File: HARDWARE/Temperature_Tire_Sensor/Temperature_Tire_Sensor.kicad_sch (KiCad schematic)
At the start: 13 parts

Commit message: A completed schematic
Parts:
- added C?: 0.1uF, Capacitor_SMD:C_0603_1608Metric, symbol SB-Spoko-Bezpieczniki-rescue:C_Small-Device
- added D?: BLUE, symbol Device:D_Small
- added FB?: 60R@100MHz, symbol Device:FerriteBead_Small
- added J?: SWD_Conn_01x06, symbol Connector:Conn_01x06_Male
- added J?: CAN_Conn_01x02, symbol Connector_Generic:Conn_01x02
- added R?: 1k, symbol Device:R_Small_US
- added R?: 1k5, Resistor_SMD:R_0603_1608Metric, symbol SB-Spoko-Bezpieczniki-rescue:R_Small-Device
- added SW?: RESET, Button_Switch_THT:SW_PUSH_6mm, symbol SB-Spoko-Bezpieczniki-rescue:SW_Push-Switch
- C? (x2): value C_Small -> 8p
- R?: value R_Small_US -> 47
- Y?: value Crystal_GND24_Small -> 16MGHz
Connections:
- net +3V3: now also FB?.1, J?.1 (Pin_1); no longer C?.1, C?.1, C?.1, C?.1, C?.1, C?.1, C?.1
- net GND: now also C?.2, J?.3 (Pin_3), R?.2, SW?.1
- net LED: now reaches U?.26 (PB0)
- net LED: now also D?.2 (A)
- net CAN_RX: now reaches U?.44 (PA11)
- net CAN_TX: now reaches U?.45 (PA12)
- net SWDIO: now reaches U?.46 (PA13)
- net SWDIO: now also J?.4 (Pin_4)
- net SWCLK: now reaches U?.49 (PA14)
- net SWCLK: now also J?.2 (Pin_2)
- net SWO: now reaches U?.55 (PB3)
- net SWO: now also J?.6 (Pin_6)
- net NRST: now reaches U?.7 (NRST)
- net NRST: now also C?.1, J?.5 (Pin_5), R?.2
- net SCL: now reaches U?.8 (PC0)
- net SDA: now reaches U?.9 (PC1)
- new net: R?.1, SW?.2
- new net: C?.1, C?.1, C?.1, C?.1, C?.1, C?.1, C?.1, FB?.2
- new net: D?.1 (K), R?.1
- new net CAN_H: J?.1 (Pin_1)
- new net CAN_L: J?.2 (Pin_2)
- no-connect marks 0 -> 41
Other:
- sheet Power Supply 3V3 2V6 ports: added none; removed RO
- note added: "CAN"
- note added: "CRYSTAL"
- note added: "DIODE"
- note added: "POWER FILTRATION"
- note added: "POWER SUPPLY"
- note added: "RESET"
- note added: "STM32"
- note added: "SWD AND CAN CONNECTORS"
- note added: "TEMPERATURE SENSOR"
- moved on the sheet: C?, R?, U?, Y?

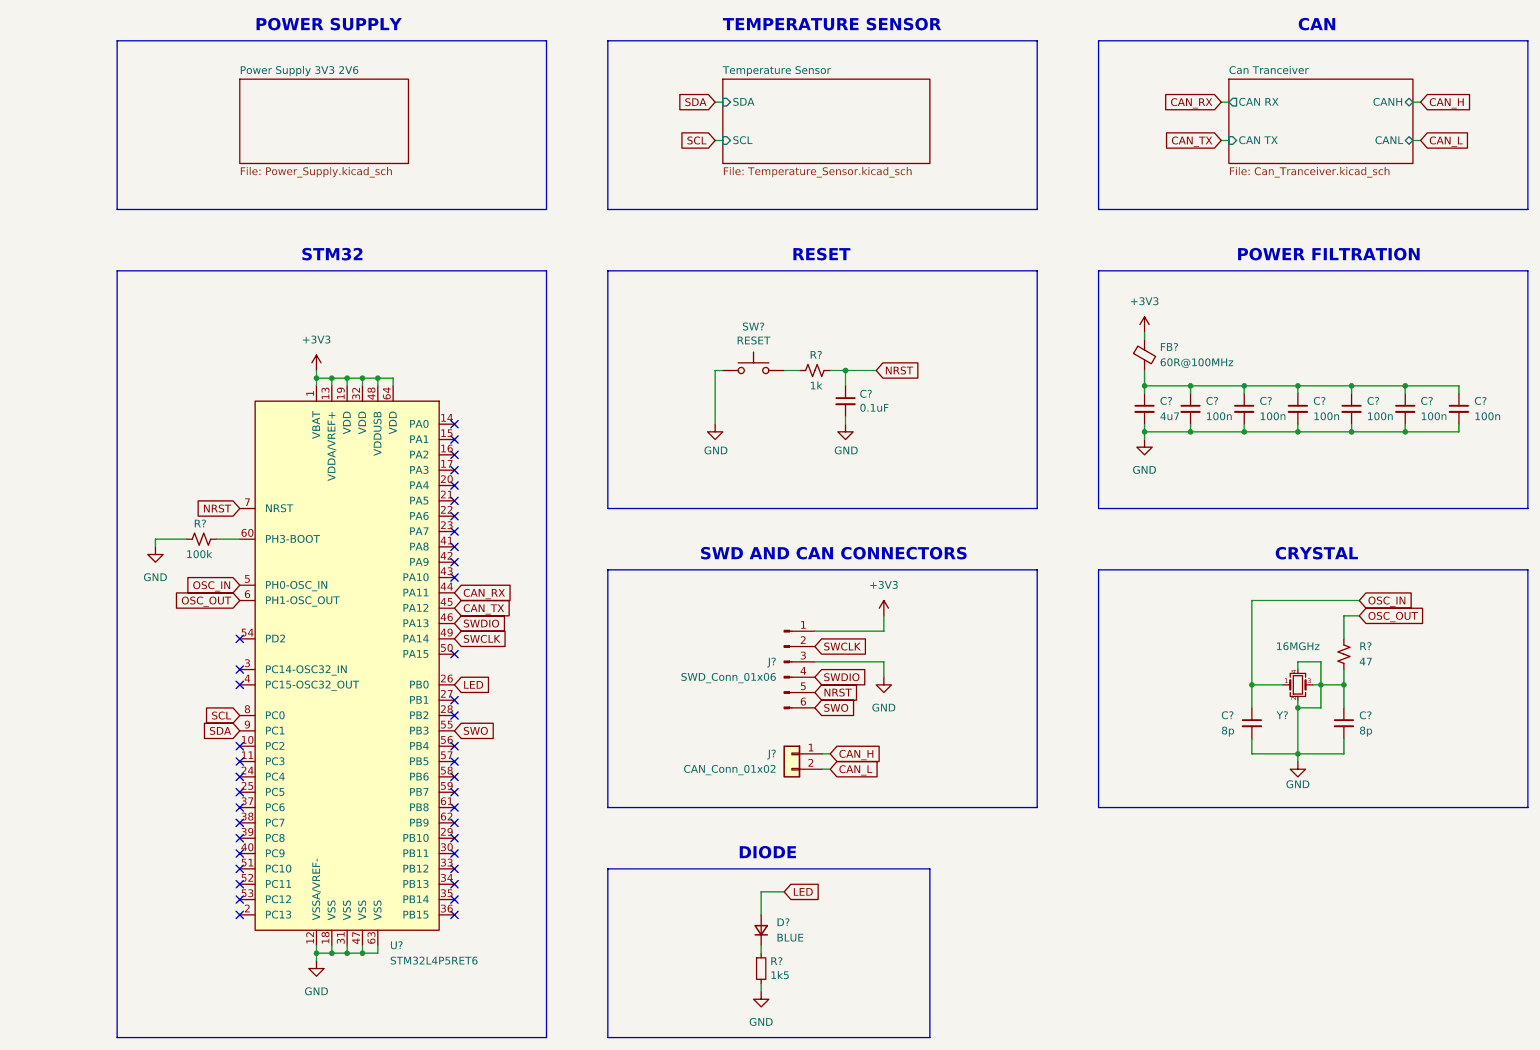
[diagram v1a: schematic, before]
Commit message: Changed the used type of labels and added power flags
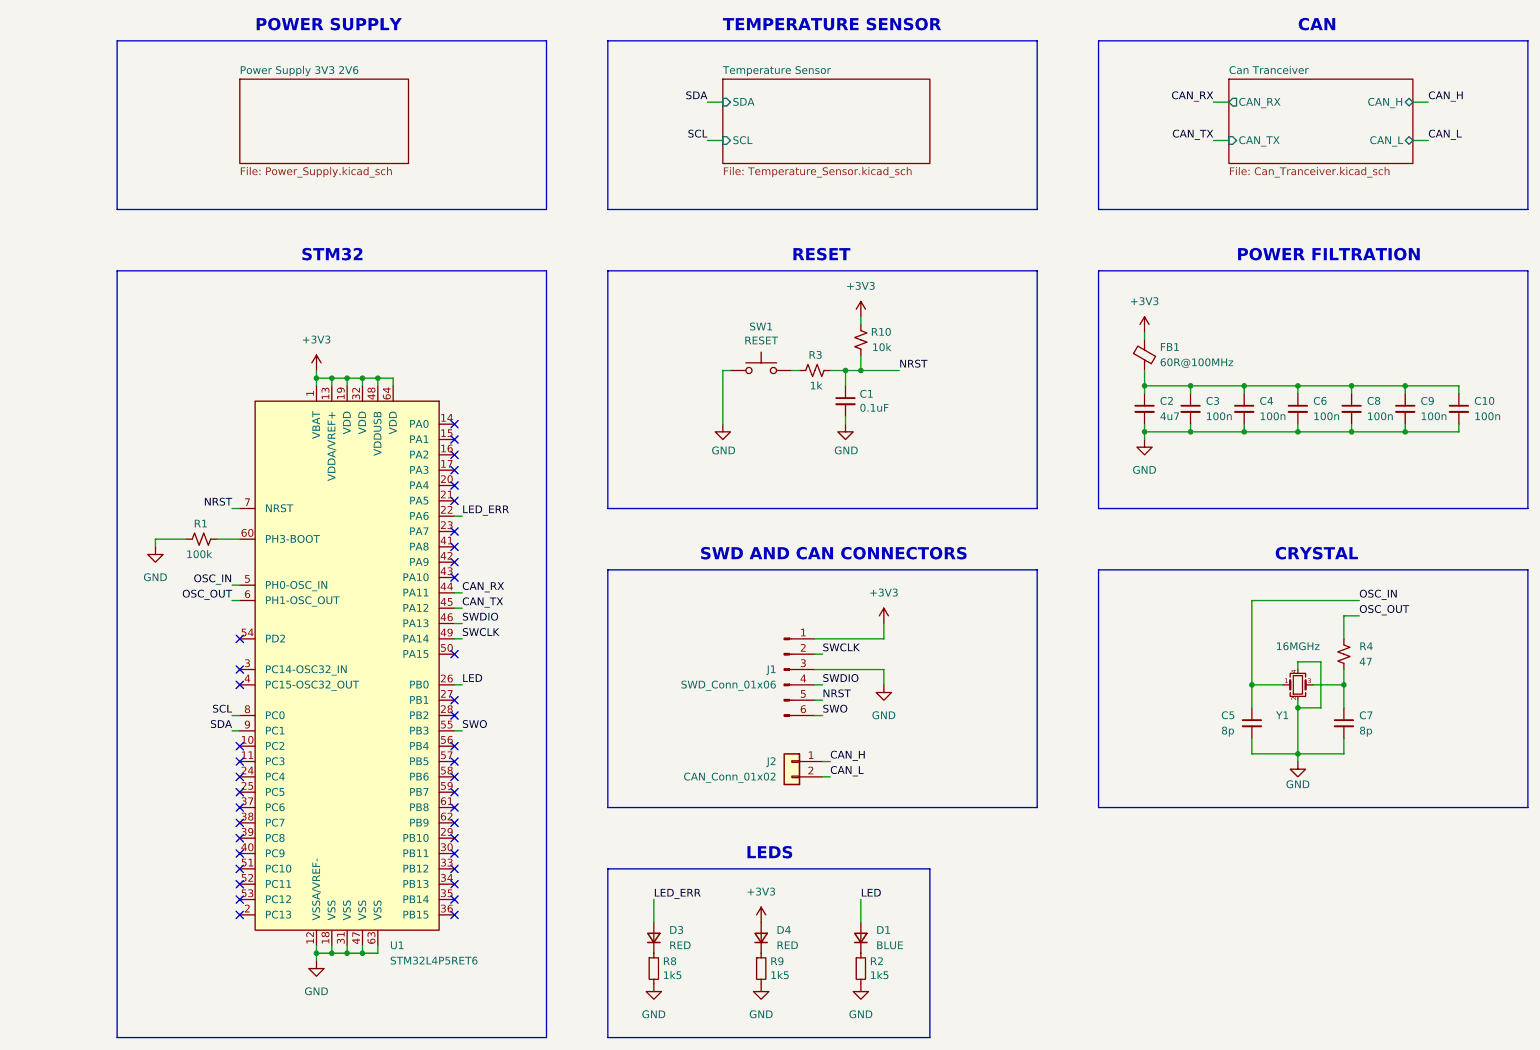
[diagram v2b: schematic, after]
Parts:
- added D3, D4: RED, symbol Device:D_Small
- added R10: 10k, symbol Device:R_Small_US
- added R8, R9: 1k5, Resistor_SMD:R_0603_1608Metric, symbol SB-Spoko-Bezpieczniki-rescue:R_Small-Device
- gave numbers to parts that had none: 21
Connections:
- net +3V3: now also D4.2 (A), R10.2
- net GND: now also R8.2, R9.2; no longer C7.1, R4.2, Y1.3
- net NRST: now also R10.1
- net LED_ERR: now reaches U1.22 (PA6)
- net LED_ERR: now also D3.2 (A)
- new net: C7.1, R4.2, Y1.3
- new net: D4.1 (K), R9.1
- new net: D3.1 (K), R8.1
- no-connect marks 41 -> 40
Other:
- sheet Can Tranceiver ports: added CAN_H, CAN_L, CAN_RX, CAN_TX; removed CAN RX, CAN TX, CANH, CANL
- note added: "LEDS"
- note removed: "DIODE"
- moved on the sheet: D1, J1, J2, R2, SW1

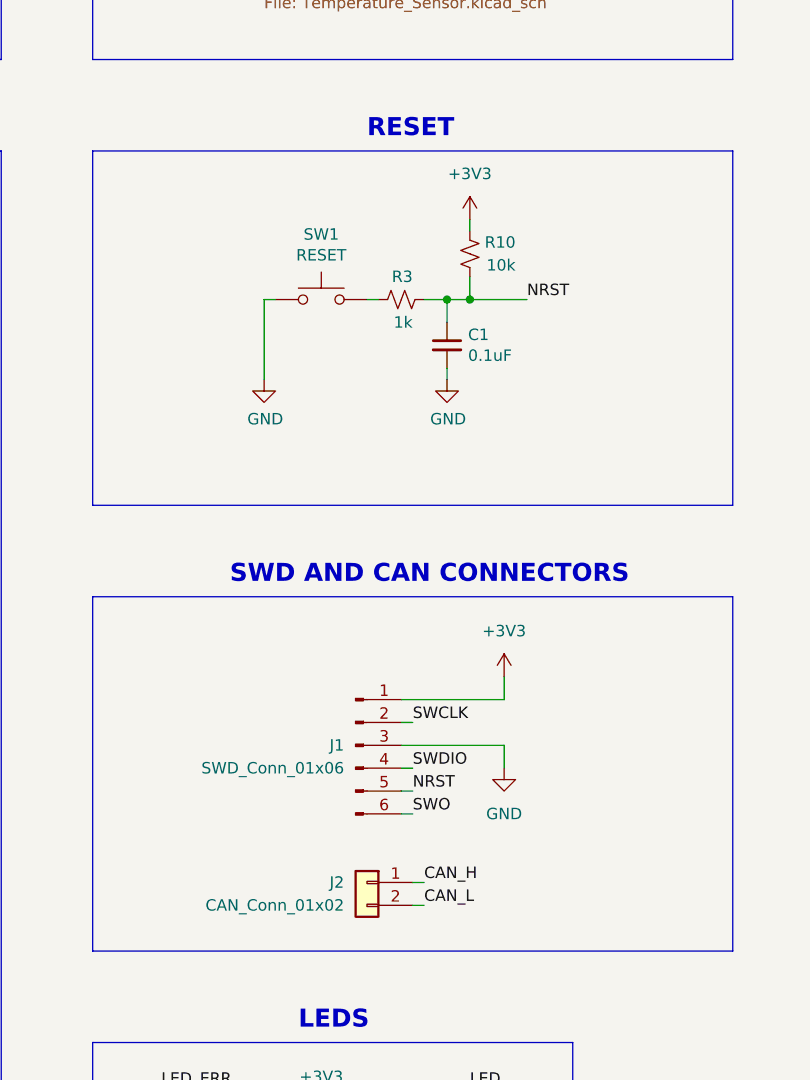
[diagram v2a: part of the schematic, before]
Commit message: Added all of the footprints
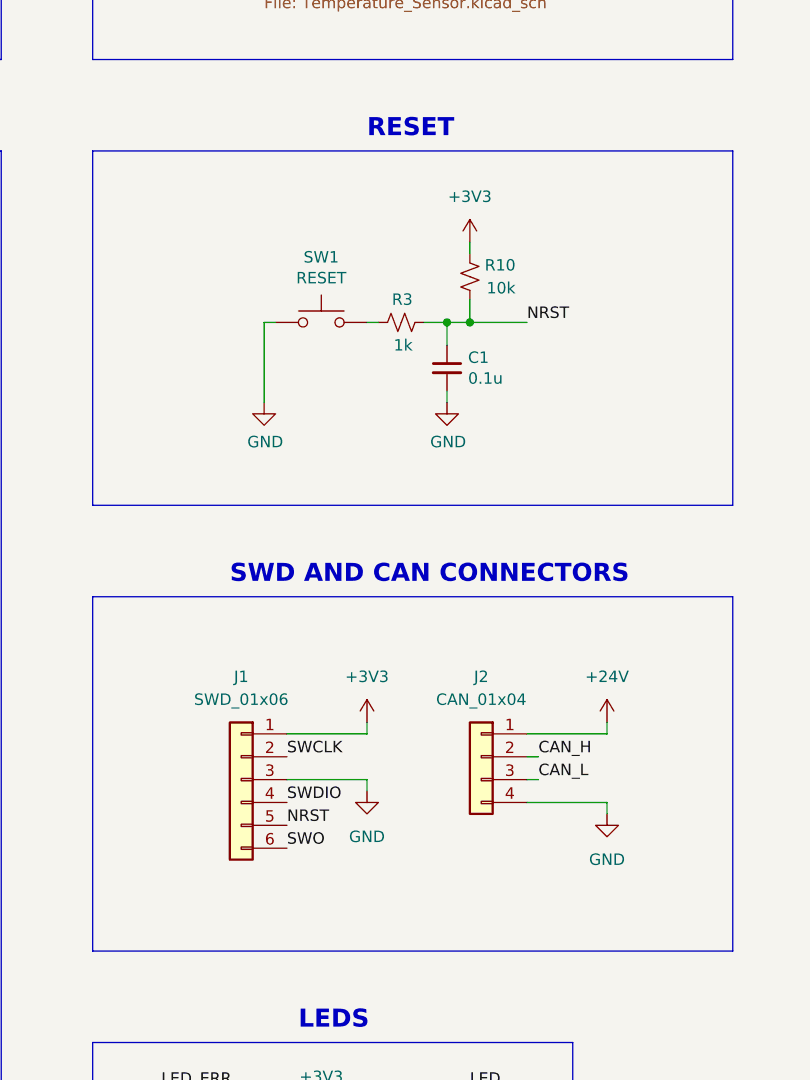
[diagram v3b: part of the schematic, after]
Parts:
- removed J1: SWD_Conn_01x06, symbol Connector:Conn_01x06_Male
- removed J2: CAN_Conn_01x02, symbol Connector_Generic:Conn_01x02
- added J1: SWD_01x06, Connector_PinHeader_2.54mm:PinHeader_1x06_P2.54mm_Vertical, symbol Connector_Generic:Conn_01x06
- added J2: CAN_01x04, SOLDER_PAD_01x04:SolderWirePad_1x04_SMD_1x2mm, symbol Connector_Generic:Conn_01x04
- C1: value 0.1uF -> 0.1u
- C10, C2, C3, C4, C6, C8, C9: footprint (none) -> Capacitor_SMD:C_0603_1608Metric
- C5, C7: footprint (none) -> Capacitor_SMD:C_0201_0603Metric
- D1, D3, D4: footprint (none) -> Diode_SMD:D_0603_1608Metric
- FB1: footprint (none) -> Inductor_SMD:L_0603_1608Metric
- R1, R10, R3, R4: footprint (none) -> Resistor_SMD:R_0603_1608Metric
- SW1: footprint Button_Switch_THT:SW_PUSH_6mm -> BUTTON:434781025816
- Y1: footprint (none) -> Crystal:Crystal_SMD_SeikoEpson_TSX3225-4Pin_3.2x2.5mm
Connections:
- net +3V3: now also J1.1 (Pin_1)
- net CAN_H: now also J2.2 (Pin_2)
- net CAN_L: now also J2.3 (Pin_3)
- net GND: now also J1.3 (Pin_3), J2.4 (Pin_4)
- net NRST: now also J1.5 (Pin_5)
- net SWCLK: now also J1.2 (Pin_2)
- net SWDIO: now also J1.4 (Pin_4)
- net SWO: now also J1.6 (Pin_6)
- new net +24V: J2.1 (Pin_1)
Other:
- moved on the sheet: C1, R10, R3, SW1

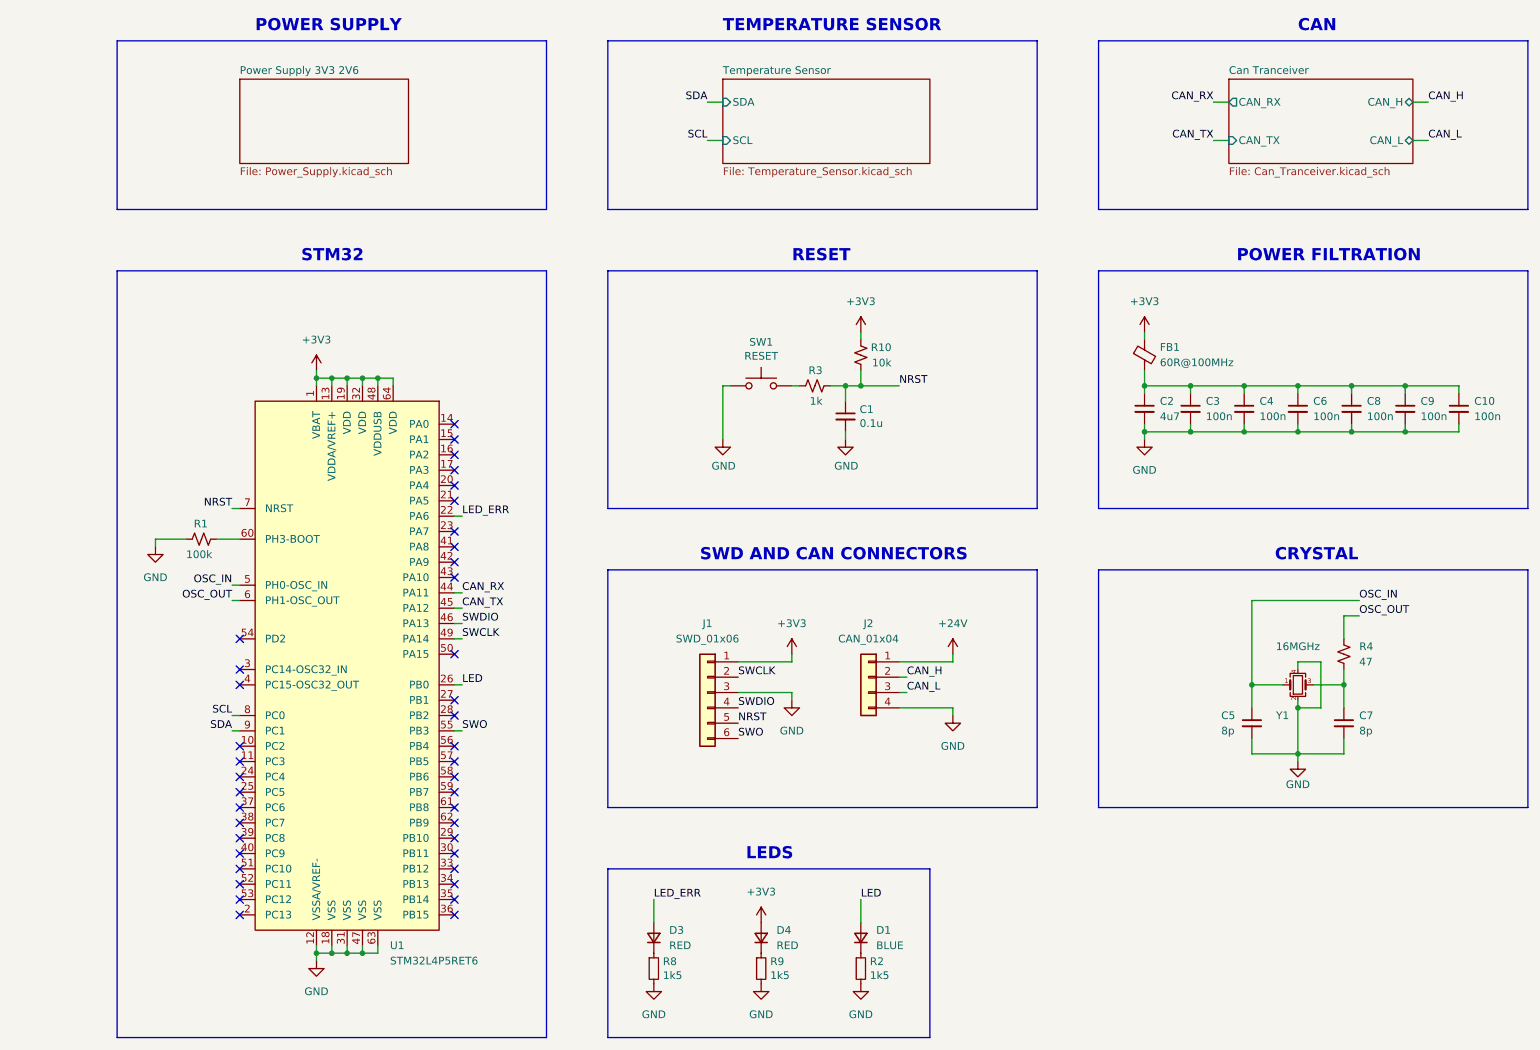
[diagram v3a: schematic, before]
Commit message: pcb layout half done
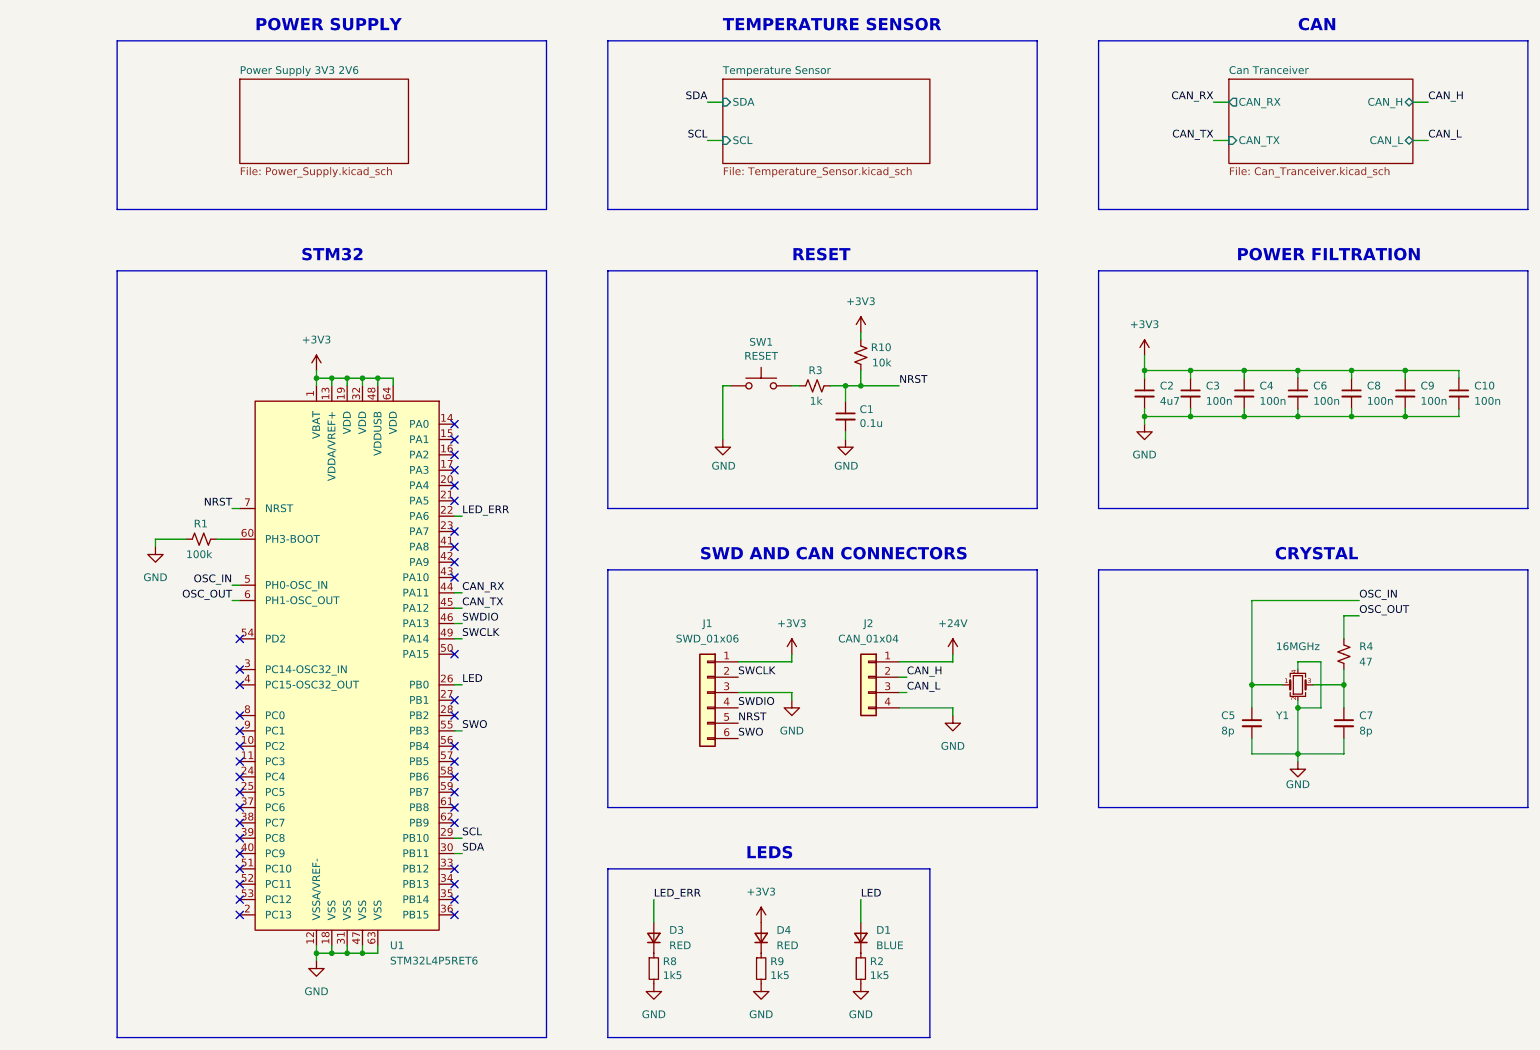
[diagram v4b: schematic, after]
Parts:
- removed FB1: 60R@100MHz, Inductor_SMD:L_0603_1608Metric, symbol Device:FerriteBead_Small
- C5, C7: footprint Capacitor_SMD:C_0201_0603Metric -> Capacitor_SMD:C_0603_1608Metric
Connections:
- net +3V3: now also C10.1, C2.1, C3.1, C4.1, C6.1, C8.1, C9.1
- net SCL: now also U1.29 (PB10); no longer U1.8 (PC0)
- net SDA: now also U1.30 (PB11); no longer U1.9 (PC1)
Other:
- moved on the sheet: C10, C2, C3, C4, C6, C8, C9
